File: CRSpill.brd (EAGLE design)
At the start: 70 x 22.2 mm, 24 parts, among them IC1 7805DT, IC2 BLUE_PILL, IC3 NCV7351D1E, J3 MA04-1, SW1 SWITCH_TACTILETOP, U1 STM32F103C8, U7 XC6206, X1 8P8C-LED

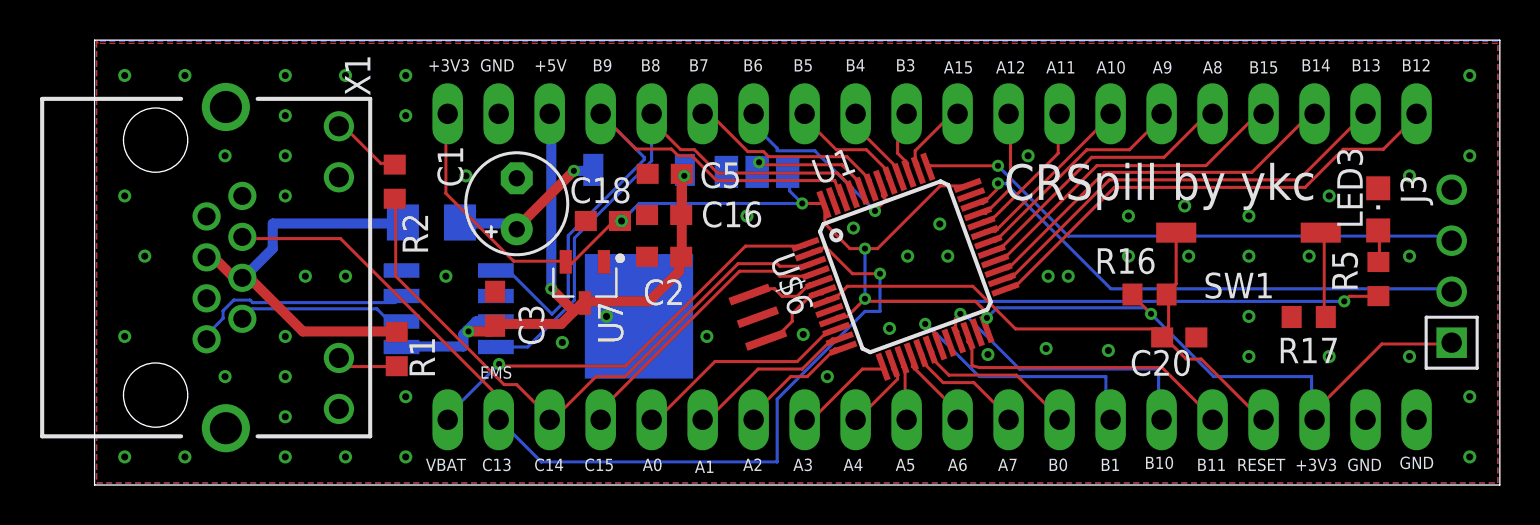
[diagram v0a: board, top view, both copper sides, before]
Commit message: 100nF add to 3V3
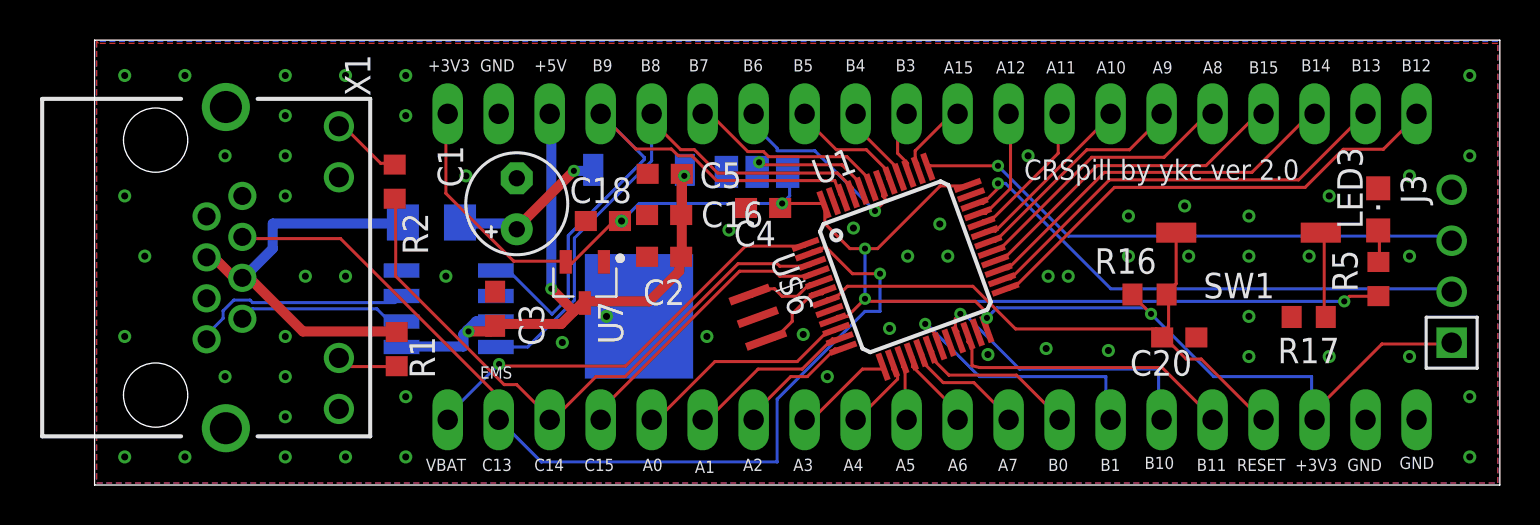
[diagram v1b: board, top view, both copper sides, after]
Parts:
- added C4: 100n, rcl:C0603
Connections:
- net +3V3: now also C4.1
- net GND: now also C4.2
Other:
- board text added: "CRSpill by ykc ver 2.0"
- board text removed: "CRSpill by ykc"
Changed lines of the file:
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@@
 <drawing>
 <settings>
-<setting alwaysvectorfont="yes"/>
+<setting alwaysvectorfont="no"/>
 <setting verticaltext="up"/>
 </settings>
@@
 <wire x1="69.5" y1="22.76" x2="-0.5" y2="22.76" width="0" layer="20"/>
 <wire x1="-0.5" y1="22.76" x2="-0.5" y2="0.6" width="0" layer="20"/>
-<text x="44.8" y="14.8" size="1.778" layer="21">CRSpill by ykc</text>
+<text x="45.8" y="15.8" size="1.016" layer="21">CRSpill by ykc ver 2.0</text>
 <text x="16.1" y="21.2" size="0.6096" layer="21">+3V3</text>
 <text x="18.7" y="21.2" size="0.6096" layer="21">GND</text>
@@
 <attribute name="VALUE" x="28.535" y="18.005" size="1.27" layer="27" rot="R180"/>
 </element>
+<element name="C4" library="rcl" library_urn="urn:adsk.eagle:library:334" package="C0603" package3d_urn="urn:adsk.eagle:package:23616/2" value="100n" x="32.8" y="14.4" smashed="yes" rot="R180">
+<attribute name="NAME" x="33.435" y="13.765" size="1.27" layer="25" rot="R180"/>
+<attribute name="SPICEPREFIX" value="C" x="32.8" y="14.4" size="1.778" layer="27" rot="R180" display="off"/>
+<attribute name="VALUE" x="33.435" y="16.305" size="1.27" layer="27" rot="R180"/>
+</element>
 </elements>
 <signals>
@@
 <via x="54" y="12" extent="1-16" drill="0.35"/>
 <via x="47" y="11" extent="1-16" drill="0.35"/>
-<via x="32" y="14" extent="1-16" drill="0.35"/>
+<via x="31.1" y="13.3" extent="1-16" drill="0.35"/>
 <via x="57" y="14" extent="1-16" drill="0.35"/>
 <via x="61" y="15" extent="1-16" drill="0.35"/>
@@
 <via x="1" y="2" extent="1-16" drill="0.35"/>
 <via x="4" y="2" extent="1-16" drill="0.35"/>
+<contactref element="C4" pad="2"/>
 </signal>
 <signal name="N$2" class="1">
@@
 <wire x1="22.875" y1="11.75" x2="22.97" y2="11.7145" width="0.1524" layer="1"/>
 <wire x1="17" y1="19" x2="17.09" y2="19.09" width="0.1524" layer="1"/>
-<wire x1="34.75" y1="14.625" x2="35.75" y2="14.625" width="0.1524" layer="1"/>
-<wire x1="34.125" y1="15.25" x2="34.75" y2="14.625" width="0.1524" layer="16"/>
-<wire x1="34.125" y1="16.125" x2="34.125" y2="15.25" width="0.1524" layer="16"/>
+<wire x1="33.75" y1="14.625" x2="35.75" y2="14.625" width="0.1524" layer="1"/>
+<wire x1="34.125" y1="15" x2="33.75" y2="14.625" width="0.1524" layer="16"/>
+<wire x1="34.125" y1="16.125" x2="34.125" y2="15" width="0.1524" layer="16"/>
 <wire x1="35.75" y1="14.625" x2="35.83515625" y2="14.570121875" width="0.1524" layer="1"/>
 <wire x1="34.125" y1="16.125" x2="34.024" y2="16.2" width="0.1524" layer="16"/>
@@
 <wire x1="37.875" y1="9.75" x2="37.875" y2="9.875" width="0.1524" layer="1"/>
 <wire x1="25.75" y1="13.75" x2="25.67" y2="13.75" width="0.1524" layer="1"/>
-<via x="34.75" y="14.625" extent="1-16" drill="0.3048"/>
+<via x="33.75" y="14.625" extent="1-16" drill="0.3048"/>
 <via x="52.125" y="9.125" extent="1-16" drill="0.3048"/>
 <via x="43.95" y="8.925" extent="1-16" drill="0.3048"/>
 <via x="37.875" y="12.375" extent="1-16" drill="0.3048"/>
 <via x="37.875" y="9.875" extent="1-16" drill="0.3048"/>
-<wire x1="34.75" y1="14.625" x2="26.625" y2="14.625" width="0.1524" layer="16"/>
+<wire x1="33.75" y1="14.625" x2="26.625" y2="14.625" width="0.1524" layer="16"/>
 <wire x1="26.625" y1="14.625" x2="25.75" y2="13.75" width="0.1524" layer="16"/>
 <via x="25.75" y="13.75" extent="1-16" drill="0.35"/>
+<contactref element="C4" pad="1"/>
+<wire x1="33.65" y1="14.4" x2="33.75" y2="14.5" width="0.1524" layer="1"/>
+<wire x1="33.75" y1="14.5" x2="33.75" y2="14.625" width="0.1524" layer="1"/>
 </signal>
 <signal name="N$9">

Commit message: シルクの追加
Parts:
- moved U$6 0.76 mm to (33.2, 9.26)
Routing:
- net N$19: track 4.09 -> 2.91 mm
- net N$2: track 20.9 -> 20.2 mm
- net N$11: track 4.08 -> 3.40 mm
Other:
- board text added: "3V3"
- board text added: "SWCLK"
- board text added: "SWDIO"
